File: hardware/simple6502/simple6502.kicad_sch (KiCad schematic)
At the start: 16 parts, among them J1 ~{VP}, J2 CLK SEL, J3 RESET, J4 6502 BUS, SW1 RESET, U1 W65C02SxP, U2 CY62256-70PC, U3 28C256, U4 DS1813-10+, X1 ACO-1MHz

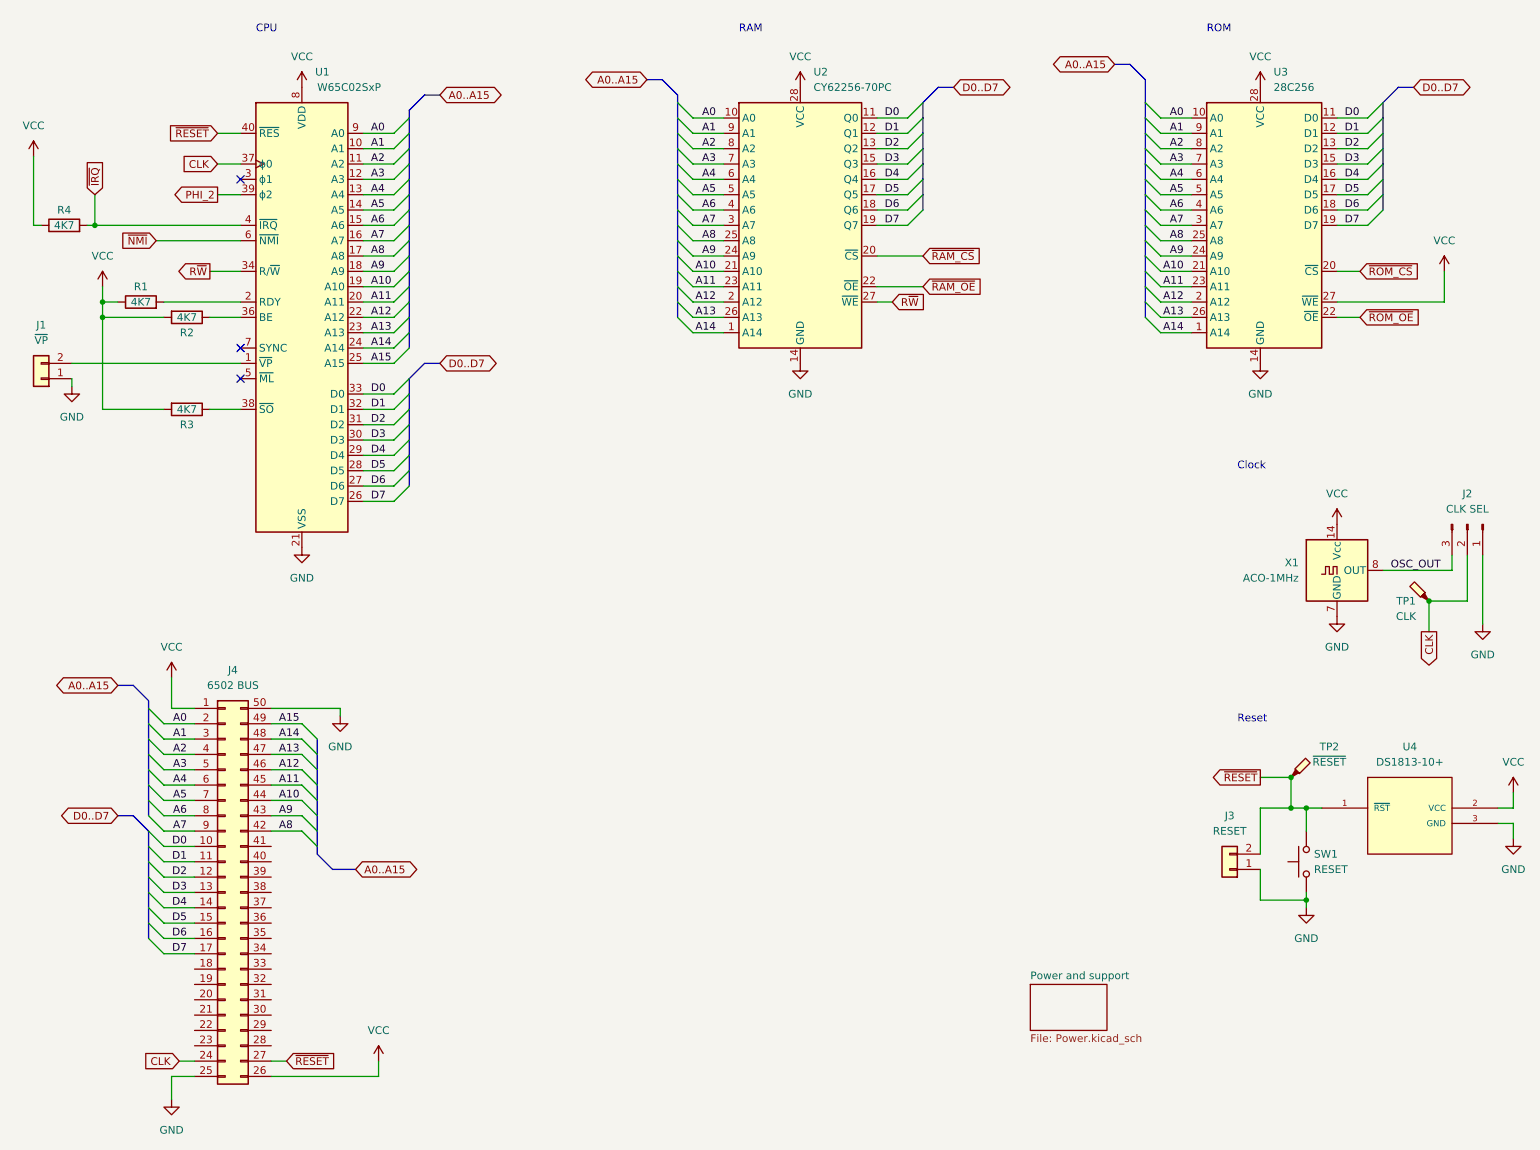
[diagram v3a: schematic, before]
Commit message: Fixed Bus label names
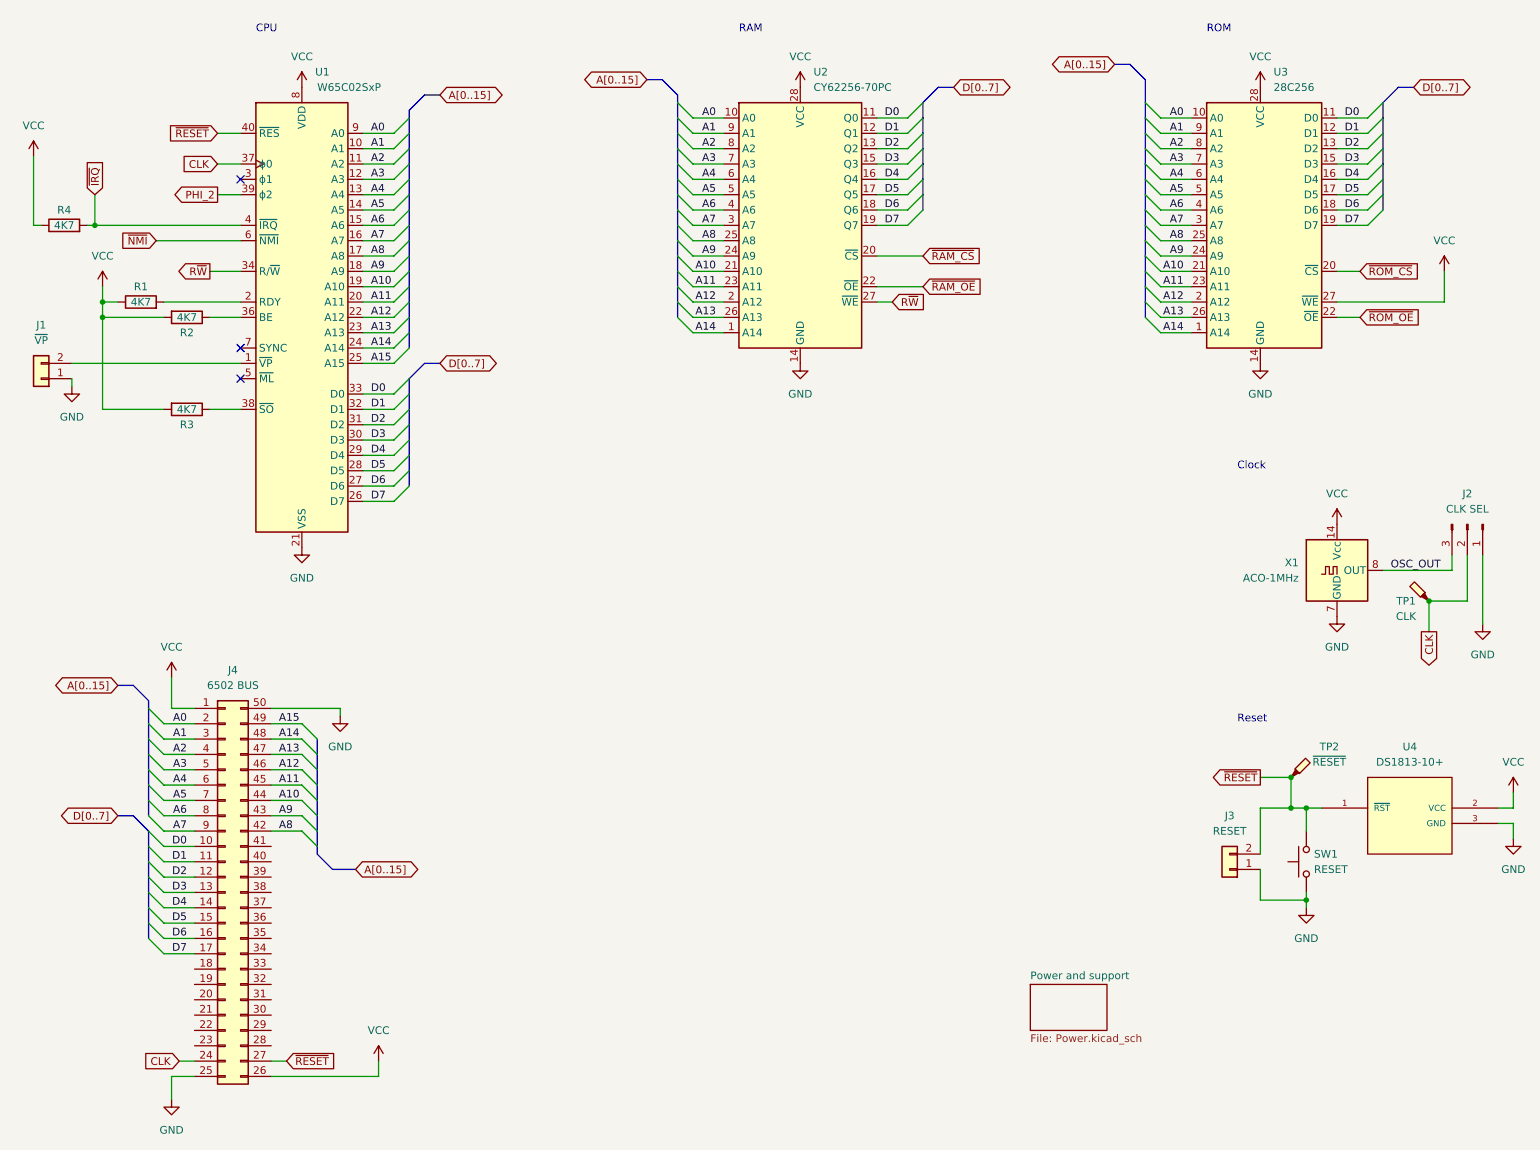
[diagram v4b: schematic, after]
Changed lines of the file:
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@@
     (effects (font (size 1.27 1.27)) (justify left bottom))
   )
-  (global_label "A0..A15" (shape tri_state) (at 29.21 125.73 180) (fields_autoplaced)
-    (effects (font (size 1.27 1.27)) (justify right))
-    (property "Intersheetrefs" "${INTERSHEET_REFS}" (at 18.0982 125.73 0)
+  (global_label "A[0..15]" (shape tri_state) (at 29.21 125.73 180) (fields_autoplaced)
+    (effects (font (size 1.27 1.27)) (justify right))
+    (property "Intersheetrefs" "${INTERSHEET_REFS}" (at 17.4934 125.73 0)
       (effects (font (size 1.27 1.27)) (justify right) hide)
     )
@@
     )
   )
-  (global_label "A0..A15" (shape tri_state) (at 116.84 25.4 180) (fields_autoplaced)
-    (effects (font (size 1.27 1.27)) (justify right))
-    (property "Intersheetrefs" "${INTERSHEET_REFS}" (at 105.7282 25.4 0)
-      (effects (font (size 1.27 1.27)) (justify right) hide)
-    )
-  )
-  (global_label "D0..D7" (shape tri_state) (at 167.64 26.67 0) (fields_autoplaced)
-    (effects (font (size 1.27 1.27)) (justify left))
-    (property "Intersheetrefs" "${INTERSHEET_REFS}" (at 177.9051 26.67 0)
-      (effects (font (size 1.27 1.27)) (justify left) hide)
-    )
-  )
-  (global_label "D0..D7" (shape tri_state) (at 29.21 147.32 180) (fields_autoplaced)
-    (effects (font (size 1.27 1.27)) (justify right))
-    (property "Intersheetrefs" "${INTERSHEET_REFS}" (at 18.9449 147.32 0)
+  (global_label "A[0..15]" (shape tri_state) (at 116.84 25.4 180) (fields_autoplaced)
+    (effects (font (size 1.27 1.27)) (justify right))
+    (property "Intersheetrefs" "${INTERSHEET_REFS}" (at 105.1234 25.4 0)
+      (effects (font (size 1.27 1.27)) (justify right) hide)
+    )
+  )
+  (global_label "D[0..7]" (shape tri_state) (at 167.64 26.67 0) (fields_autoplaced)
+    (effects (font (size 1.27 1.27)) (justify left))
+    (property "Intersheetrefs" "${INTERSHEET_REFS}" (at 178.3285 26.67 0)
+      (effects (font (size 1.27 1.27)) (justify left) hide)
+    )
+  )
+  (global_label "D[0..7]" (shape tri_state) (at 29.21 147.32 180) (fields_autoplaced)
+    (effects (font (size 1.27 1.27)) (justify right))
+    (property "Intersheetrefs" "${INTERSHEET_REFS}" (at 18.5215 147.32 0)
       (effects (font (size 1.27 1.27)) (justify right) hide)
     )
@@
     )
   )
-  (global_label "A0..A15" (shape tri_state) (at 82.55 27.94 0) (fields_autoplaced)
-    (effects (font (size 1.27 1.27)) (justify left))
-    (property "Intersheetrefs" "${INTERSHEET_REFS}" (at 93.6618 27.94 0)
-      (effects (font (size 1.27 1.27)) (justify left) hide)
-    )
-  )
-  (global_label "D0..D7" (shape tri_state) (at 243.84 26.67 0) (fields_autoplaced)
-    (effects (font (size 1.27 1.27)) (justify left))
-    (property "Intersheetrefs" "${INTERSHEET_REFS}" (at 254.1051 26.67 0)
+  (global_label "A[0..15]" (shape tri_state) (at 82.55 27.94 0) (fields_autoplaced)
+    (effects (font (size 1.27 1.27)) (justify left))
+    (property "Intersheetrefs" "${INTERSHEET_REFS}" (at 94.2666 27.94 0)
+      (effects (font (size 1.27 1.27)) (justify left) hide)
+    )
+  )
+  (global_label "D[0..7]" (shape tri_state) (at 243.84 26.67 0) (fields_autoplaced)
+    (effects (font (size 1.27 1.27)) (justify left))
+    (property "Intersheetrefs" "${INTERSHEET_REFS}" (at 254.5285 26.67 0)
       (effects (font (size 1.27 1.27)) (justify left) hide)
     )
@@
     )
   )
-  (global_label "A0..A15" (shape tri_state) (at 194.31 22.86 180) (fields_autoplaced)
-    (effects (font (size 1.27 1.27)) (justify right))
-    (property "Intersheetrefs" "${INTERSHEET_REFS}" (at 183.1982 22.86 0)
+  (global_label "A[0..15]" (shape tri_state) (at 194.31 22.86 180) (fields_autoplaced)
+    (effects (font (size 1.27 1.27)) (justify right))
+    (property "Intersheetrefs" "${INTERSHEET_REFS}" (at 182.5934 22.86 0)
       (effects (font (size 1.27 1.27)) (justify right) hide)
     )
@@
     )
   )
-  (global_label "D0..D7" (shape tri_state) (at 82.55 72.39 0) (fields_autoplaced)
-    (effects (font (size 1.27 1.27)) (justify left))
-    (property "Intersheetrefs" "${INTERSHEET_REFS}" (at 92.8151 72.39 0)
+  (global_label "D[0..7]" (shape tri_state) (at 82.55 72.39 0) (fields_autoplaced)
+    (effects (font (size 1.27 1.27)) (justify left))
+    (property "Intersheetrefs" "${INTERSHEET_REFS}" (at 93.2385 72.39 0)
       (effects (font (size 1.27 1.27)) (justify left) hide)
     )
@@
     )
   )
-  (global_label "A0..A15" (shape tri_state) (at 68.58 156.21 0) (fields_autoplaced)
-    (effects (font (size 1.27 1.27)) (justify left))
-    (property "Intersheetrefs" "${INTERSHEET_REFS}" (at 79.6918 156.21 0)
+  (global_label "A[0..15]" (shape tri_state) (at 68.58 156.21 0) (fields_autoplaced)
+    (effects (font (size 1.27 1.27)) (justify left))
+    (property "Intersheetrefs" "${INTERSHEET_REFS}" (at 80.2966 156.21 0)
       (effects (font (size 1.27 1.27)) (justify left) hide)
     )
@@
     )
   )
-  (symbol (lib_id "Device:R") (at 20.32 49.53 90) (unit 1)
+  (symbol (lib_name "R_2") (lib_id "Device:R") (at 20.32 49.53 90) (unit 1)
     (in_bom yes) (on_board yes) (dnp no) (fields_autoplaced)
     (property "Reference" "R4" (at 20.32 46.99 90)

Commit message: Memory decoder v1
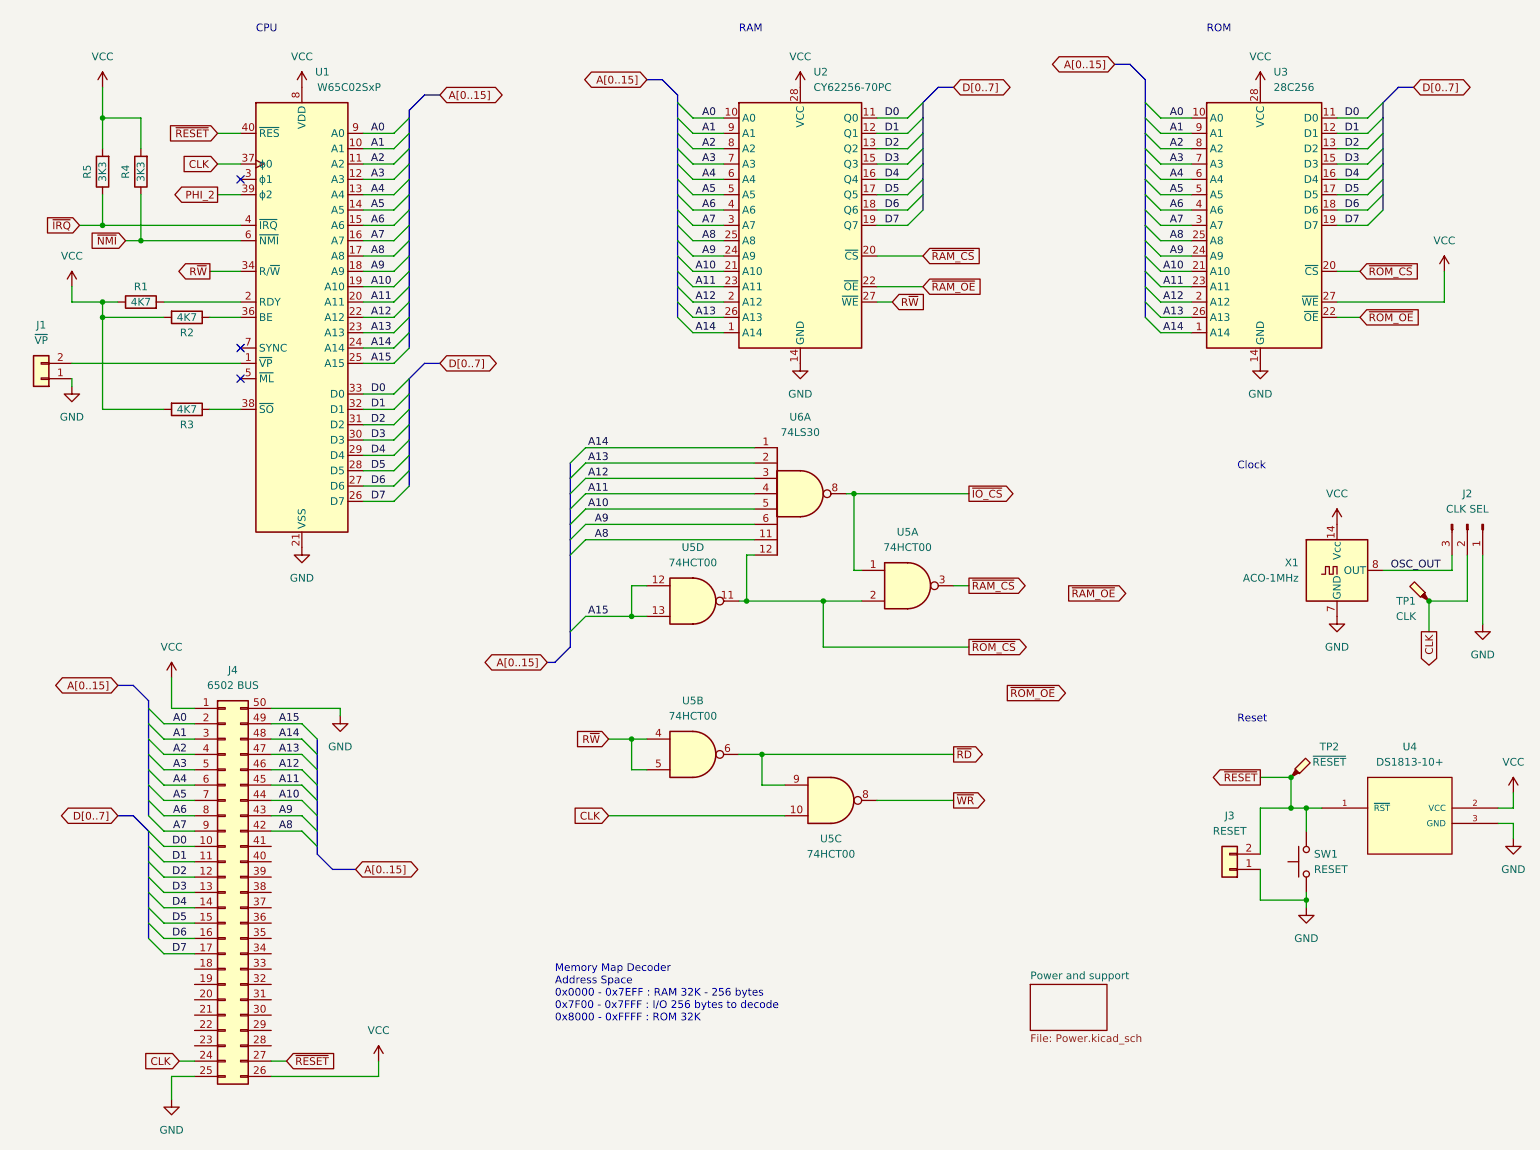
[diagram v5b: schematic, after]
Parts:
- added R5: 3K3, symbol Device:R
- added U5: 74HCT00, symbol 74xx:74HCT00
- added U6: 74LS30, symbol 74xx:74LS30
- R4: value 4K7 -> 3K3
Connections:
- net A10: now also U6.5
- net A11: now also U6.4
- net A12: now also U6.3
- net A13: now also U6.2
- net A14: now also U6.1
- net A15: now also U5.12, U5.13
- net A8: now also U6.11
- net A9: now also U6.6
- net CLK: now also U5.10
- net R~{W}: now also U5.4, U5.5
- net VCC: now also R4.2, R5.2; no longer R4.1
- net ~{IRQ}: now also R5.1; no longer R4.2
- net ~{NMI}: now also R4.1
- net ~{RAM_CS}: now also U5.3
- net ~{ROM_CS}: now also U5.11, U5.2, U6.12
- new net ~{IO_CS}: U5.1, U6.8
- new net ~{RD}: U5.6, U5.9
- new net ~{WR}: U5.8
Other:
- note added: "Memory Map Decoder Address Space 0x0000 - 0x7EFF : RAM 32K - 256 bytes 0x7F00 - 0x7FFF : I/O 256 bytes to decode 0x8000 - 0xFFFF : ROM 32K"

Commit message: Main board schematic complete v0.0.1
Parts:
- added TP3: ~{RESET}, symbol Connector:TestPoint_Probe
- TP2: value ~{RESET} -> PHI_2
- renumbered R5 to R1, R4 to R2, R1 to R3, R2 to R4, R3 to R5, U4 to T1, U6 to U4
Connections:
- net ~{RAM_OE} is gone; now on net ~{RD}: U2.22 (~{OE})
- net ~{ROM_OE} is gone; now on net ~{RD}: U3.22 (~{OE})
- net GND: now also J2.3 (Pin_3), J3.2 (Pin_2), J4.39 (Pin_39); no longer J2.1 (Pin_1), J3.1 (Pin_1)
- net OSC_OUT: now also J2.1 (Pin_1); no longer J2.3 (Pin_3)
- net PHI_2: now also TP2.1
- net R~{W}: no longer U2.27 (~{WE})
- net ~{IO_CS}: now also J4.36 (Pin_36)
- net ~{IRQ}: now also J4.23 (Pin_23)
- net ~{NMI}: now also J4.28 (Pin_28)
- net ~{RAM_CS}: now also J4.38 (Pin_38)
- net ~{RD}: now also J4.41 (Pin_41)
- net ~{RESET}: now also J3.1 (Pin_1), TP3.1; no longer J3.2 (Pin_2), TP2.1
- net ~{ROM_CS}: now also J4.37 (Pin_37)
- net ~{WR}: now also J4.40 (Pin_40), U2.27 (~{WE})
- no-connect marks 3 -> 15
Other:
- moved on the sheet: J1, J2, J3, R1, R2, R3, R4, R5, SW1, T1, U1
